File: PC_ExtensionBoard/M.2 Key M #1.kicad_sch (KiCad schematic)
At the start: 14 parts, among them J5 Bus_M.2_MDT180M03001

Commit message: components placement R1
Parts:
- removed A2: Mech_M2_2280_H2.5mm, antmicro-footprints:Mech_M2_2280_H2.5mm, symbol antmicroModules:Mech_M2_2280_H2.5mm
- removed C71, C72, C73, C74: C_22u_16V_0603, antmicro-footprints:C_0603_1608Metric, symbol antmicroCapacitors0603:C_22u_16V_0603
- removed D13: LED_G_0603_LTST-C190GKT, antmicro-footprints:LED_0603_1608Metric_G, symbol antmicroLEDIndicationDiscrete:LED_G_0603_LTST-C190GKT
- removed H2: Spacer_Drill3.7mm_H2.5mm_9774025151R, antmicro-footprints:Spacer_Drill3.7mm_H2.5mm_9774025151R, symbol antmicroMechanicalParts:Spacer_Drill3.7mm_H2.5mm_9774025151R
- removed J5: Bus_M.2_MDT180M03001, antmicro-footprints:Bus_M.2_Socket_Key_M_Amphenol_MDT180M03001, symbol antmicroPciConnectors:Bus_M.2_MDT180M03001
- removed R120, R124: R_0R_0402, antmicro-footprints:R_0402_1005Metric, symbol antmicroResistors0402:R_0R_0402
- removed R121, R122: R_10k_0402, antmicro-footprints:R_0402_1005Metric, symbol antmicroResistors0402:R_10k_0402
- removed R123: R_220R_0402, antmicro-footprints:R_0402_1005Metric, symbol antmicroResistors0402:R_220R_0402
- removed R125: R_0R_22.4A_0603, antmicro-footprints:R_0603_1608Metric, symbol antmicroResistors0603:R_0R_22.4A_0603
- added A1: Mech_M2_2280_H2.5mm, PC_Components_1:Mech_M2_2280_H2.5mm, symbol antmicroModules:Mech_M2_2280_H2.5mm
- added C75, C76, C77, C78: C_22u_16V_0603, PC_Components_1:C_0603_1608Metric, symbol antmicroCapacitors0603:C_22u_16V_0603
- added D21: LED_G_0603_LTST-C190GKT, PC_Components_1:LED_0603_1608Metric_G, symbol antmicroLEDIndicationDiscrete:LED_G_0603_LTST-C190GKT
- added H1: Spacer_Drill3.7mm_H2.5mm_9774025151R, PC_Components_1:Spacer_Drill3.7mm_H2.5mm_9774025151R, symbol antmicroMechanicalParts:Spacer_Drill3.7mm_H2.5mm_9774025151R
- added J8: Bus_M.2_1-2199230-6, PC_Components_1:Bus_M.2_Socket_Key_M_TE_1-2199230-6, symbol antmicroPciConnectors:Bus_M.2_1-2199230-6
- added R126, R130: R_0R_0402, PC_Components_1:R_0402_1005Metric, symbol antmicroResistors0402:R_0R_0402
- added R127, R128: R_10k_0402, PC_Components_1:R_0402_1005Metric, symbol antmicroResistors0402:R_10k_0402
- added R129: R_220R_0402, PC_Components_1:R_0402_1005Metric, symbol antmicroResistors0402:R_220R_0402
- added R131: R_0R_22.4A_0603, PC_Components_1:R_0603_1608Metric, symbol antmicroResistors0603:R_0R_22.4A_0603
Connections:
- net +3V3: now also R127.2, R128.2, R129.2, R131.2
- net GND: now also C75.1, C76.1, C77.1, C78.1, H1.1, J8.1 (GND), J8.15 (GND), J8.21 (GND), J8.27 (GND), J8.3 (GND), J8.33 (GND), J8.39 (GND), J8.45 (GND), J8.51 (GND), J8.57 (GND), J8.71 (GND), J8.73 (GND), J8.75 (GND), J8.9 (GND), J8.MP1 (MP), J8.MP2 (MP)
- net M2_3V3: now also C75.2, C76.2, C77.2, C78.2, J8.12 (3V3), J8.14 (3V3), J8.16 (3V3), J8.18 (3V3), J8.2 (3V3), J8.4 (3V3), J8.70 (3V3), J8.72 (3V3), J8.74 (3V3), R131.1
- net PCIE_{REF}.CK+: now also J8.55 (REFCLK_P)
- net PCIE_{REF}.CK-: now also J8.53 (REFCLK_N)
- net PCIe_{x4}.RX0+: now also J8.41 (PER0_N)
- net PCIe_{x4}.RX0-: now also J8.43 (PER0_P)
- net PCIe_{x4}.RX1+: now also J8.29 (PER1_N)
- net PCIe_{x4}.RX1-: now also J8.31 (PER1_P)
- net PCIe_{x4}.RX2+: now also J8.17 (PER2_N)
- net PCIe_{x4}.RX2-: now also J8.19 (PER2_P)
- net PCIe_{x4}.RX3+: now also J8.5 (PER3_N)
- net PCIe_{x4}.RX3-: now also J8.7 (PER3_P)
- net PCIe_{x4}.TX0+: now also J8.47 (PET0_N)
- net PCIe_{x4}.TX0-: now also J8.49 (PET0_P)
- net PCIe_{x4}.TX1+: now also J8.35 (PET1_N)
- net PCIe_{x4}.TX1-: now also J8.37 (PET1_P)
- net PCIe_{x4}.TX2+: now also J8.23 (PET2_N)
- net PCIe_{x4}.TX2-: now also J8.25 (PET2_P)
- net PCIe_{x4}.TX3+: now also J8.11 (PET3_N)
- net PCIe_{x4}.TX3-: now also J8.13 (PET3_P)
- net SUSCLK: now also R130.2
- net ~{CLKREQ}: now also J8.52 (~{CLKREQ}), R128.1
- net ~{PERST_D}: now also J8.50 (~{PERST}), R126.2, R127.1
- net ~{PERST}: now also R126.1
- new net: D21.2 (A), R129.1
- new net: J8.68 (SUSCLK), R130.1
- new net: D21.1 (C), J8.10 (LED)

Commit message: refactor project
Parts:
- A1: symbol antmicroModules:Mech_M2_2280_H2.5mm -> A_PC_ExtensionBoard:Mech_M2_2280_H2.5mm
- C75, C76, C77, C78: symbol antmicroCapacitors0603:C_22u_16V_0603 -> A_PC_ExtensionBoard:C_22u_16V_0603
- D21: symbol antmicroLEDIndicationDiscrete:LED_G_0603_LTST-C190GKT -> A_PC_ExtensionBoard:LED_G_0603_LTST-C190GKT; Public (none) -> False
- H1: symbol antmicroMechanicalParts:Spacer_Drill3.7mm_H2.5mm_9774025151R -> A_PC_ExtensionBoard:Spacer_Drill3.7mm_H2.5mm_9774025151R; Manufacturer (none) -> Würth Elektronik; Public (none) -> False
- J8: footprint PC_Components_1:Bus_M.2_Socket_Key_M_TE_1-2199230-6 -> (none); symbol antmicroPciConnectors:Bus_M.2_1-2199230-6 -> A_PC_ExtensionBoard:Bus_M.2_1-2199230-6
- R126: footprint PC_Components_1:R_0402_1005Metric -> antmicro-footprints:R_0402_1005Metric; symbol antmicroResistors0402:R_0R_0402 -> A_PC_ExtensionBoard:R_0R_0402; Author (none) -> Antmicro; License (none) -> Apache-2.0; Public (none) -> False
- R127, R128: footprint PC_Components_1:R_0402_1005Metric -> antmicro-footprints:R_0402_1005Metric; symbol antmicroResistors0402:R_10k_0402 -> A_PC_ExtensionBoard:R_10k_0402; Author (none) -> Antmicro; License (none) -> Apache-2.0; Manufacturer (none) -> Bourns; Public (none) -> False
- R129: symbol antmicroResistors0402:R_220R_0402 -> A_PC_ExtensionBoard:R_220R_0402
- R130: footprint PC_Components_1:R_0402_1005Metric -> antmicro-footprints:R_0402_1005Metric; symbol antmicroResistors0402:R_0R_0402 -> A_PC_ExtensionBoard:R_0R_0402; Author (none) -> Antmicro; License (none) -> Apache-2.0; Manufacturer (none) -> Panasonic; Public (none) -> False
- R131: symbol antmicroResistors0603:R_0R_22.4A_0603 -> A_PC_ExtensionBoard:R_0R_22.4A_0603
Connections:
- net +3V3 renamed +3.3V

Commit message: re-link symbol
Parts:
- R126, R127, R128, R130: footprint antmicro-footprints:R_0402_1005Metric -> PC_Components_1:R_0402_1005Metric
- renumbered H1 to H10
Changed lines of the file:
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@@
 		(in_pos_files yes)
 		(dnp no)
-		(property "Reference" "H1"
+		(property "Reference" "H10"
 			(at 130.81 161.29 0)
 			(show_name no)
@@
 			(project "PC_ExtensionBoard"
 				(path "/6f8c8ec7-fa36-4248-8716-390866a3d0b0/e0373dc5-8a62-4a52-9d01-906bea33f6b6"
-					(reference "H1")
+					(reference "H10")
 					(unit 1)
 				)
@@
 			)
 		)
-		(property "Footprint" "antmicro-footprints:R_0402_1005Metric"
+		(property "Footprint" "PC_Components_1:R_0402_1005Metric"
 			(at 118.11 31.75 0)
 			(hide yes)
@@
 			)
 		)
-		(property "Footprint" "antmicro-footprints:R_0402_1005Metric"
+		(property "Footprint" "PC_Components_1:R_0402_1005Metric"
 			(at 166.37 81.28 0)
 			(hide yes)
@@
 			)
 		)
-		(property "Footprint" "antmicro-footprints:R_0402_1005Metric"
+		(property "Footprint" "PC_Components_1:R_0402_1005Metric"
 			(at 92.71 68.58 0)
 			(hide yes)
@@
 			)
 		)
-		(property "Footprint" "antmicro-footprints:R_0402_1005Metric"
+		(property "Footprint" "PC_Components_1:R_0402_1005Metric"
 			(at 109.22 31.75 0)
 			(hide yes)

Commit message: update LCSC Number
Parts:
- R126: Author Antmicro -> (none); Current 1A -> (none); LCSC (none) -> C242160; License Apache-2.0 -> (none); Public False -> (none)
- R130: Author Antmicro -> (none); Current 1A -> (none); LCSC (none) -> C242160; License Apache-2.0 -> (none); Manufacturer Panasonic -> (none); Public False -> (none)
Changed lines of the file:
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@@
 			)
 		)
-		(property "Tolerance" ""
-			(at 166.37 76.2 0)
-			(hide yes)
-			(show_name no)
-			(do_not_autoplace no)
-			(effects
-				(font
-					(size 1.27 1.27)
-				)
-				(justify left bottom)
-			)
-		)
-		(property "Current" "1A"
-			(at 166.37 96.52 0)
-			(hide yes)
-			(show_name no)
-			(do_not_autoplace no)
-			(effects
-				(font
-					(size 1.27 1.27)
-					(thickness 0.15)
-				)
-				(justify left bottom)
-			)
-		)
-		(property "Manufacturer" "Panasonic"
-			(at 166.37 88.9 0)
-			(hide yes)
-			(show_name no)
-			(do_not_autoplace no)
-			(effects
-				(font
-					(size 1.27 1.27)
-					(thickness 0.15)
-				)
-				(justify left bottom)
-			)
-		)
-		(property "License" "Apache-2.0"
-			(at 166.37 91.44 0)
-			(hide yes)
-			(show_name no)
-			(do_not_autoplace no)
-			(effects
-				(font
-					(size 1.27 1.27)
-					(thickness 0.15)
-				)
-				(justify left bottom)
-			)
-		)
-		(property "Author" "Antmicro"
-			(at 166.37 93.98 0)
-			(hide yes)
-			(show_name no)
-			(do_not_autoplace no)
-			(effects
-				(font
-					(size 1.27 1.27)
-					(thickness 0.15)
-				)
-				(justify left bottom)
-			)
-		)
-		(property "Public" "False"
-			(at 166.37 96.52 0)
-			(hide yes)
-			(show_name no)
-			(do_not_autoplace no)
-			(effects
-				(font
-					(size 1.27 1.27)
-				)
-				(justify left bottom)
+		(property "LCSC" "C242160"
+			(at 146.05 66.04 0)
+			(hide yes)
+			(show_name no)
+			(do_not_autoplace no)
+			(effects
+				(font
+					(size 1.27 1.27)
+				)
 			)
 		)
@@
 			)
 		)
-		(property "Tolerance" ""
-			(at 92.71 63.5 0)
-			(hide yes)
-			(show_name no)
-			(do_not_autoplace no)
-			(effects
-				(font
-					(size 1.27 1.27)
-				)
-				(justify left bottom)
-			)
-		)
-		(property "Current" "1A"
-			(at 92.71 83.82 0)
-			(hide yes)
-			(show_name no)
-			(do_not_autoplace no)
-			(effects
-				(font
-					(size 1.27 1.27)
-					(thickness 0.15)
-				)
-				(justify left bottom)
-			)
-		)
-		(property "License" "Apache-2.0"
-			(at 92.71 78.74 0)
-			(hide yes)
-			(show_name no)
-			(do_not_autoplace no)
-			(effects
-				(font
-					(size 1.27 1.27)
-					(thickness 0.15)
-				)
-				(justify left bottom)
-			)
-		)
-		(property "Author" "Antmicro"
-			(at 92.71 81.28 0)
-			(hide yes)
-			(show_name no)
-			(do_not_autoplace no)
-			(effects
-				(font
-					(size 1.27 1.27)
-					(thickness 0.15)
-				)
-				(justify left bottom)
-			)
-		)
-		(property "Public" "False"
-			(at 92.71 83.82 0)
-			(hide yes)
-			(show_name no)
-			(do_not_autoplace no)
-			(effects
-				(font
-					(size 1.27 1.27)
-				)
-				(justify left bottom)
-			)
-		)
+		(property "LCSC" "C242160"
+			(at 72.39 53.34 0)
+			(hide yes)
+			(show_name no)
+			(do_not_autoplace no)
+			(effects
+				(font
+					(size 1.27 1.27)
+				)
+			)
+		)

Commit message: update Schematic
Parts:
- added R82, R83: R_10k_0402, PC_Components_1:R_0402_1005Metric, symbol A_PC_ExtensionBoard:R_10k_0402
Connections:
- net GND: now also R83.2
- new net +3V3: R82.1
- new net PCIE1-4_SATA_PCIE: R82.2, R83.1

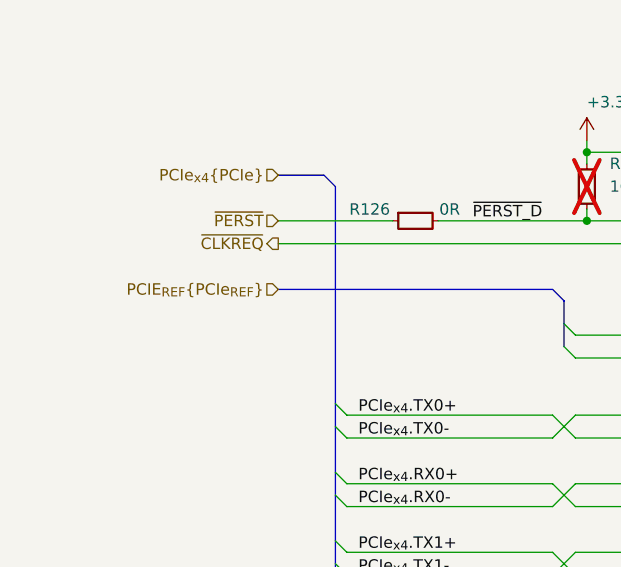
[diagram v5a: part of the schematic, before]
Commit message: update diff pair routing
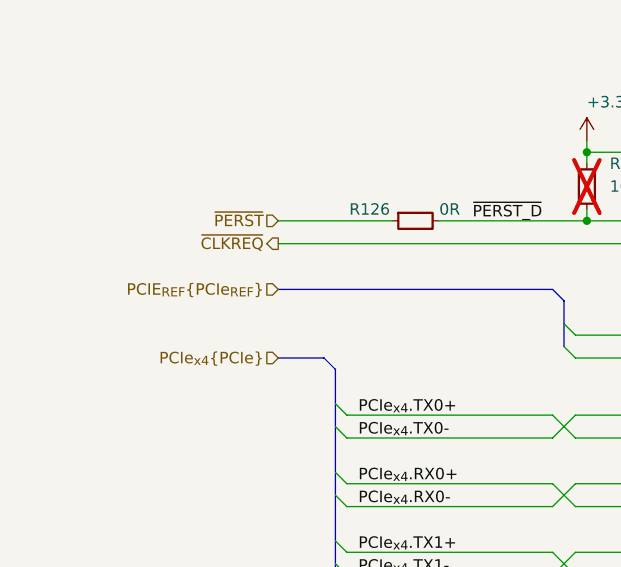
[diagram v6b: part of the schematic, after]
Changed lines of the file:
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@@
 	(bus
 		(pts
-			(xy 66.04 49.53) (xy 64.77 48.26)
+			(xy 66.04 69.85) (xy 64.77 68.58)
 		)
 		(stroke
@@
 	(bus
 		(pts
-			(xy 59.69 48.26) (xy 64.77 48.26)
+			(xy 59.69 68.58) (xy 64.77 68.58)
 		)
 		(stroke
@@
 	(bus
 		(pts
-			(xy 66.04 49.53) (xy 66.04 73.66)
+			(xy 66.04 69.85) (xy 66.04 73.66)
 		)
 		(stroke
@@
 	(hierarchical_label "PCIe_{x4}{PCIe}"
 		(shape input)
-		(at 59.69 48.26 180)
-		(effects
-			(font
+		(at 59.69 68.58 180)
+		(effects
+			(font
